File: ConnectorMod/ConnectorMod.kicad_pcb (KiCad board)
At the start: 2 copper layers, 98.5 x 90 mm, 82 parts, among them J1 PJ-325, J10 VIN, J11 VCC, J12 MRX, J13 MTX, J14 DACL, J15 DACR, J16 DACG, J17 VSW, J2 PJ-325, J3 PJ-325, J4 PJ-066A, J5 BAT1, J6 BAT2, J7 AMP, J8 GNDA, J9 GND, Q1 MMBT3904, Q2 MMBT3904, Q3 MMBT3906, U1 TLP2366, U2 74LVC1G08, U3 TLV2372

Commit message: Remove loud jumper and tweak filter values
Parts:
- removed the C13 at (79.0, 77.5)
- removed the JP7 at (71.5, 74.5)
- removed JP8: LOUD_R, project-parts:SolderJumper_Custom
- removed the R19 at (67.0, 82.0)
- removed the R20 at (54.0, 82.0)
- removed the R21 at (78.0, 74.5)
- removed the R22 at (80.0, 74.5)
- added C8: 330p, Capacitor_SMD:C_0603_1608Metric, F.Cu at (66.5, 86.0)
- added C9: 330p, Capacitor_SMD:C_0603_1608Metric, F.Cu at (54.5, 86.0)
- C6, C7: value 1n -> 330p
- moved R16 45.7 mm to (98.0, 72.0), turned to 0 degrees
- moved R15 29.8 mm to (91.5, 72.0), turned to 180 degrees
- moved C6 0.50 mm to (66.5, 84.0)
- moved C7 0.50 mm to (54.5, 84.0)
- renumbered C8 to C10, C9 to C11, C10 to C12, C11 to C13, C12 to C15, JP9 to JP7, R17 to R15, R18 to R16, R15 to R17, R16 to R18, R23 to R19, R24 to R20, R25 to R21, R26 to R22, R27 to R23, R28 to R24
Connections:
- C12 pad 1: Net-(C10-Pad1) -> Net-(U3A--)
- C12 pad 2: Net-(C10-Pad2) -> Net-(C12-Pad2)
- C13 pad 1: Net-(C11-Pad1) -> Net-(U3B--)
- C13 pad 2: Net-(C11-Pad2) -> Net-(C13-Pad2)
- C6 pad 1: Net-(C10-Pad1) -> Net-(U3A--)
- C7 pad 1: Net-(C11-Pad1) -> Net-(U3B--)
- R13 pad 1: Net-(C10-Pad2) -> Net-(C12-Pad2)
- R14 pad 1: Net-(C11-Pad2) -> Net-(C13-Pad2)
- R15 pad 1: Net-(C10-Pad1) -> Net-(C12-Pad2)
- R15 pad 2: Net-(U3A--) -> GNDA
- R16 pad 1: Net-(C11-Pad1) -> Net-(C13-Pad2)
- R16 pad 2: Net-(U3B--) -> GNDA
- U3 pad 1: Net-(C10-Pad1) -> Net-(U3A--)
- U3 pad 7: Net-(C11-Pad1) -> Net-(U3B--)
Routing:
- net Net-(C11-Pad1): track 52.4 -> 0.00 mm
- net Net-(U3B--): track 7.52 -> 55.3 mm
- net Net-(C10-Pad1): track 34.7 -> 0.00 mm
- net Net-(U3A--): track 7.38 -> 37.2 mm
- net Net-(JP8-A): track 18.6 -> 0.00 mm, vias 2 -> 0
- net /VCENT: track 15.4 -> 0.00 mm
- net Net-(C13-Pad2): track 0.00 -> 10.4 mm
- net Net-(JP7-A): track 7.89 -> 0.00 mm
- net +3.3VA: track 48.7 -> 41.4 mm
- net Net-(C12-Pad2): track 0.00 -> 7.32 mm
- net Net-(C11-Pad2): track 4.72 -> 0.00 mm
- net Net-(C10-Pad2): track 4.72 -> 0.00 mm
- net +6V: track 77.5 -> 75.5 mm
- net Net-(C7-Pad2): track 7.99 -> 9.49 mm
- net Net-(C6-Pad2): track 7.99 -> 9.49 mm
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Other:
- board text added: "${TITLE} ${REVISION}"
- board text removed: "${TITLE} v${REVISION}"
- board text removed: "LOUD"

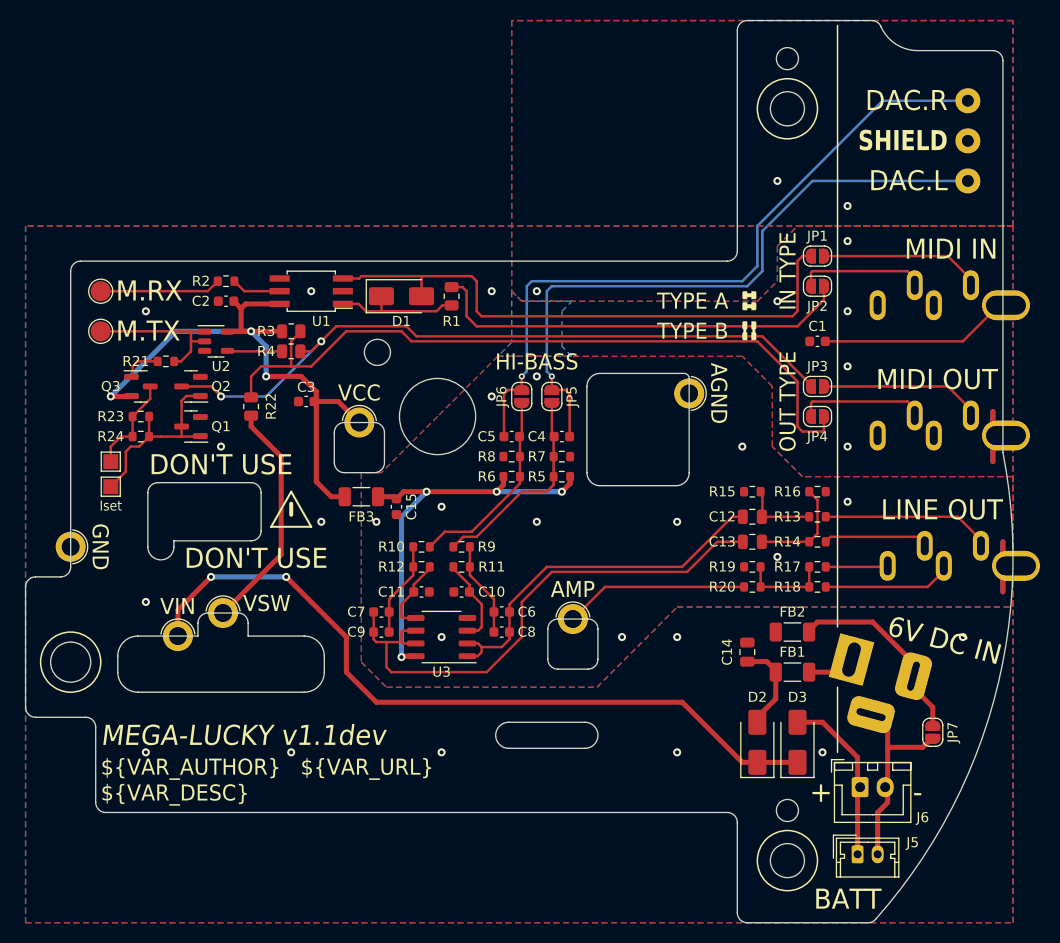
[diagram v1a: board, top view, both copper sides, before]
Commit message: Adjust outline and holes
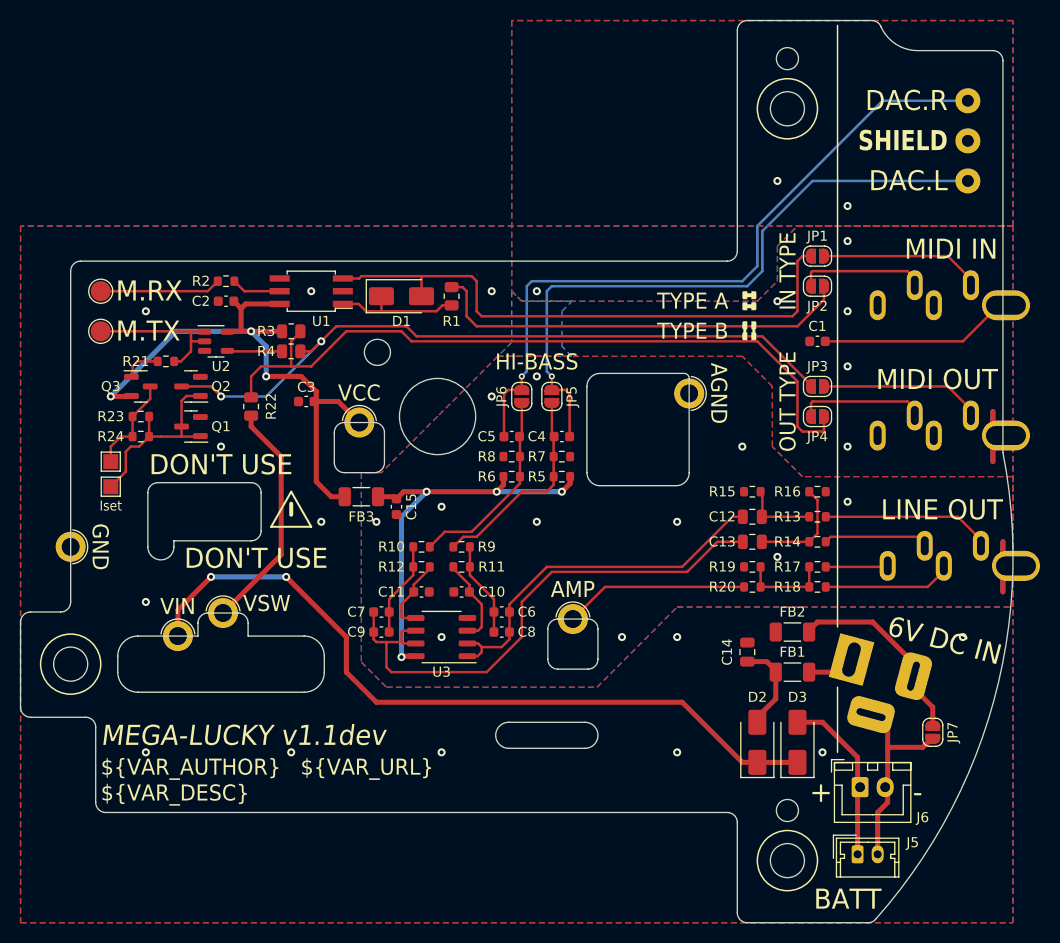
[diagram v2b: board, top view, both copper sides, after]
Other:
- board size 98.5 x 90 mm -> 99 x 90 mm

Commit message: Change MIDI type jumpers to cross pads
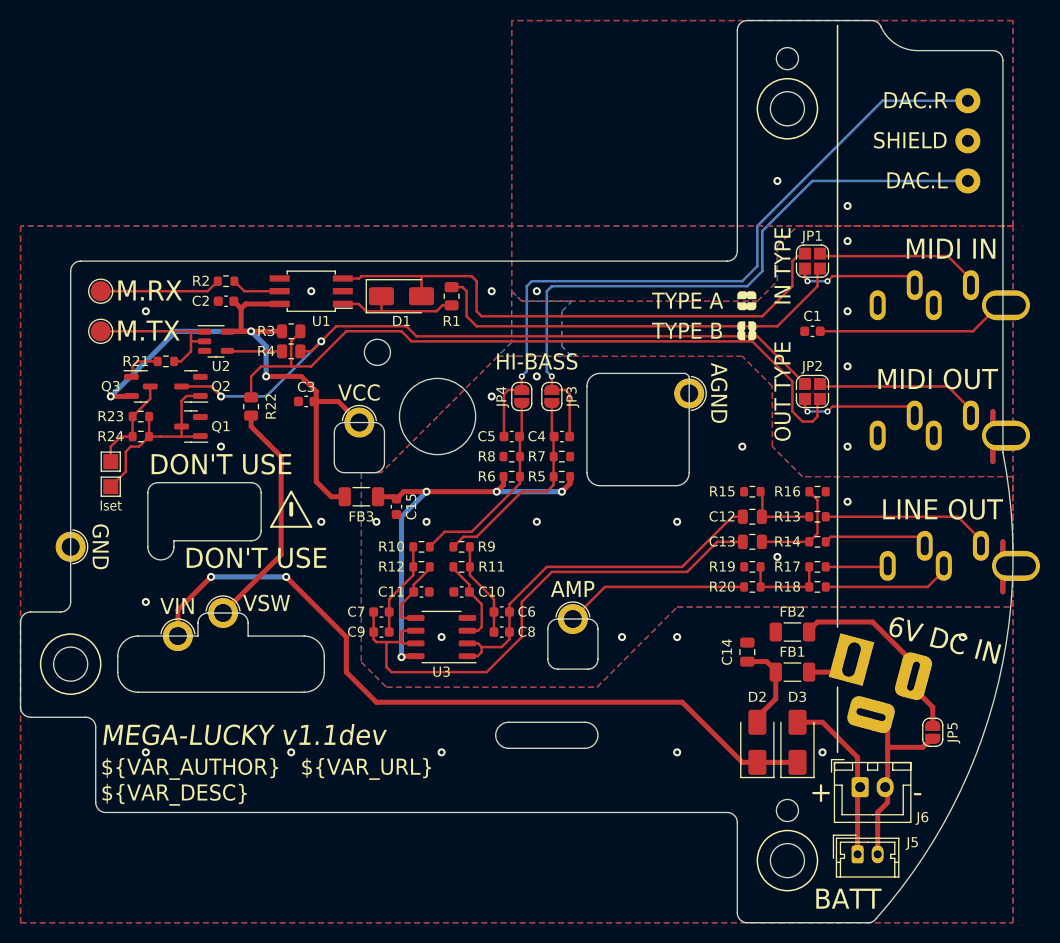
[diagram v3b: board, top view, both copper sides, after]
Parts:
- removed the JP3 at (98.0, 61.5)
- removed the JP4 at (98.0, 64.5)
- JP1: value MIT -> XMI; footprint project-parts:SolderJumper_Custom -> project-parts:SolderJumper_Cross
- JP2: value MIR -> XMO; footprint project-parts:SolderJumper_Custom -> project-parts:SolderJumper_Cross
- moved JP2 10.5 mm to (97.5, 62.0)
- moved C1 1.12 mm to (97.5, 56.0)
- moved JP1 0.71 mm to (97.5, 49.0)
- renumbered JP5 to JP3, JP6 to JP4, JP7 to JP5
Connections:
- net /MIN_G renamed Net-(C1-Pad1)
- JP2 pad 1: /MIN_R -> /MOUT_SINK
- JP2 pad 2: /MIN_SRC -> /MOUT_T
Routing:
- net /MIN_SINK: track 57.6 -> 55.7 mm
- net /MOUT_SRC: track 73.2 -> 71.9 mm
- net /MOUT_SINK: track 71.2 -> 70.4 mm
- net /MOUT_T: track 16.2 -> 16.7 mm
- net /MIN_T: track 16.2 -> 16.7 mm
- net /MIN_R: vias 0 -> 2
- net /MOUT_R: vias 0 -> 2
- net GND: vias 18 -> 17

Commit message: Use protected source/sink for MIDI out
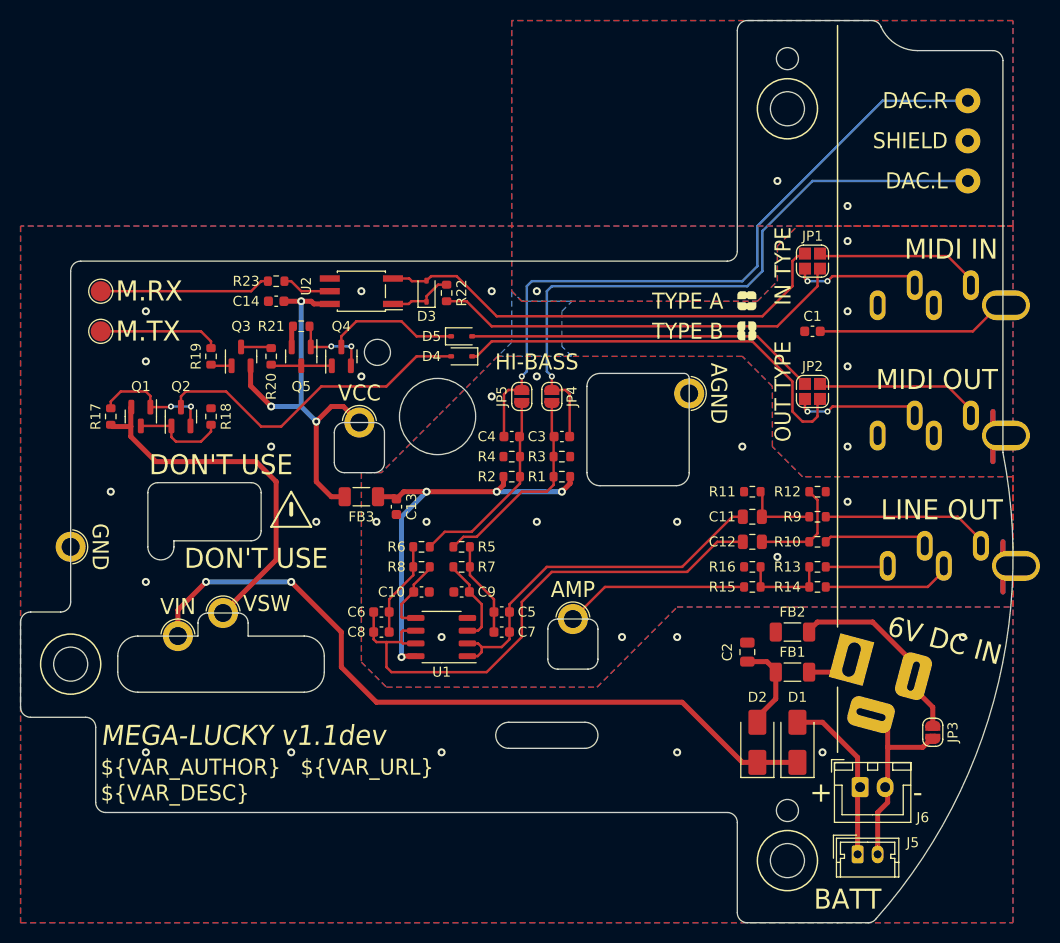
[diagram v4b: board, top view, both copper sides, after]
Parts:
- removed the C3 at (47.0, 63.0)
- removed the D1 at (56.5, 52.5)
- removed the R1 at (61.5, 52.5)
- removed the R23 at (30.5, 64.5)
- removed the R3 at (45.5, 56.0)
- removed the R4 at (45.5, 58.0)
- removed TP1, TP2: Iset, TestPoint:TestPoint_Pad_1.5x1.5mm
- removed the U2 at (38.0, 57.0)
- added D3: BAT54WS, Diode_SMD:D_SOD-323, F.Cu at (59.0, 52.0)
- added D4: BAT54WS, Diode_SMD:D_SOD-323, F.Cu at (62.5, 58.5)
- added D5: BAT54WS, Diode_SMD:D_SOD-323, F.Cu at (62.5, 56.5)
- added Q2: MMBT3906, Package_TO_SOT_SMD:SOT-23, F.Cu at (34.5, 64.5)
- added Q3: MMBT3906, Package_TO_SOT_SMD:SOT-23, F.Cu at (40.5, 58.5)
- added R17: 100R, Resistor_SMD:R_0603_1608Metric, F.Cu at (27.5, 64.5)
- added R18: 10K, Resistor_SMD:R_0603_1608Metric, F.Cu at (37.5, 64.5)
- added R20: 10K, Resistor_SMD:R_0603_1608Metric, F.Cu at (43.5, 58.5)
- R21: renamed from R24; value 1K -> 100R
- R22: footprint Resistor_SMD:R_0805_2012Metric -> Resistor_SMD:R_0603_1608Metric
- U2: renamed from U1; footprint Package_SO:SO-6_4.4x3.6mm_P1.27mm -> Package_SO:SO-5_4.4x3.6mm_P1.27mm
- moved R22 22.6 mm to (61.0, 52.2)
- moved R21 19.4 mm to (46.5, 55.5), turned to 180 degrees
- moved Q4 15.3 mm to (50.5, 58.5), turned to 90 degrees
- moved Q5 13.0 mm to (46.5, 58.5), turned to -90 degrees
- moved C14 5.00 mm to (44.0, 53.0)
- moved R23 5.00 mm to (44.0, 51.0)
- moved U2 5.00 mm to (52.5, 52.0)
- moved R19 4.53 mm to (37.5, 58.5), turned to -90 degrees
- moved Q1 3.00 mm to (30.5, 64.5), turned to -90 degrees
- renumbered C11 to C10, C12 to C11, C13 to C12, C15 to C13, C2 to C14, C14 to C2, C4 to C3, C5 to C4, C6 to C5, C7 to C6, C8 to C7, C9 to C8, C10 to C9, D3 to D1, JP5 to JP3, JP3 to JP4, JP4 to JP5, J7 to PAD1, J15 to PAD10, J16 to PAD11, J8 to PAD2, J9 to PAD3, J10 to PAD4, J11 to PAD5, J17 to PAD6, J12 to PAD7, J13 to PAD8, J14 to PAD9, Q3 to Q1, Q2 to Q4, Q1 to Q5, R5 to R1, R14 to R10, R15 to R11, R16 to R12, R17 to R13, R18 to R14, R20 to R15, R19 to R16, R21 to R19, R6 to R2, R2 to R23, R7 to R3, R8 to R4, R9 to R5, R10 to R6, R11 to R7, R12 to R8, R13 to R9, U3 to U1
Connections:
- Q1 pad 1: Net-(Q3-B) -> Net-(Q1-B)
- Q1 pad 2: +3.3V -> +VSW
- Q1 pad 3: Net-(Q3-C) -> Net-(Q1-C)
- Q4 pad 1: Net-(Q1-B) -> Net-(Q4-B)
- Q4 pad 2: GND -> Net-(Q4-E)
- Q4 pad 3: /MOUT_SINK -> Net-(D5-K)
- Q5 pad 1: Net-(Q1-B) -> Net-(Q4-E)
- Q5 pad 3: Net-(Q1-B) -> Net-(Q4-B)
- R21 pad 1: Net-(Q3-C) -> Net-(Q4-E)
- R21 pad 2: Net-(Q1-B) -> GND
- R22 pad 1: +VSW -> /MIN_SRC
- R22 pad 2: /MOUT_SRC -> Net-(D3-K)
- R23 pad 1: Net-(R2-Pad1) -> (no net)
- U2 pad 1: /MIN_SD -> Net-(D3-K)
- U2 pad 5: Net-(R2-Pad1) -> Net-(R23-Pad1)
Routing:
- net /MOUT_SINK: track 70.4 -> 35.2 mm, vias 2 -> 0
- net Net-(D4-A): track 0.00 -> 32.6 mm
- net /MOUT_SRC: track 71.9 -> 42.2 mm
- net +3.3V: track 60.4 -> 40.3 mm
- net +VSW: track 23.3 -> 36.7 mm
- net Net-(D5-K): track 0.00 -> 13.3 mm
- net /MIN_SD: track 12.9 -> 0.00 mm
- net Net-(Q1-C): track 0.00 -> 9.39 mm
- net /MIN_SINK: track 55.7 -> 47.1 mm
- net Net-(Q4-E): track 0.00 -> 8.15 mm, vias 0 -> 2
- net Net-(Q1-B): track 19.9 -> 12.4 mm, vias 0 -> 2
- net Net-(Q3-C): track 9.82 -> 3.05 mm
- net Net-(D3-K): track 0.00 -> 6.51 mm
- net Net-(Q4-B): track 0.00 -> 6.10 mm
- net Net-(R4-Pad1): track 5.47 -> 0.00 mm
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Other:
- board text removed: "Iset"

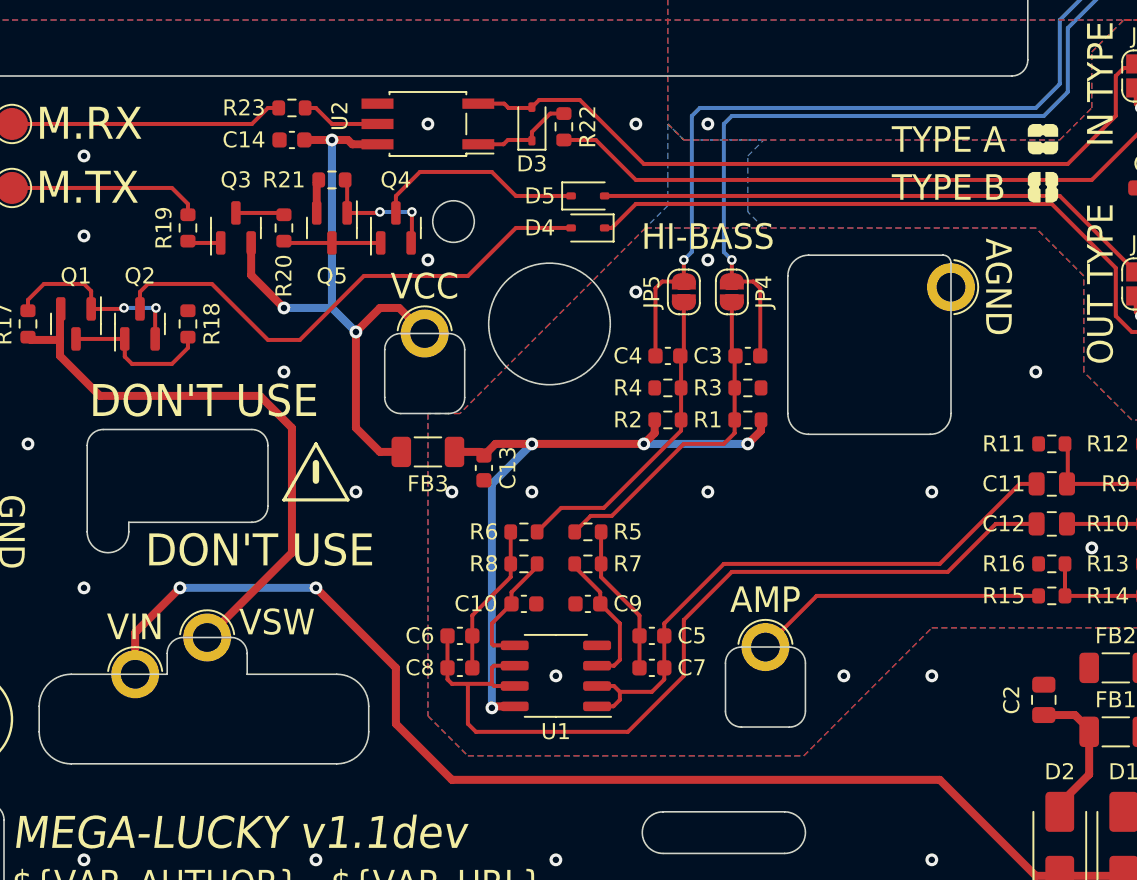
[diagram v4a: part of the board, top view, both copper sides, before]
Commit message: Tidy up opamp circuit
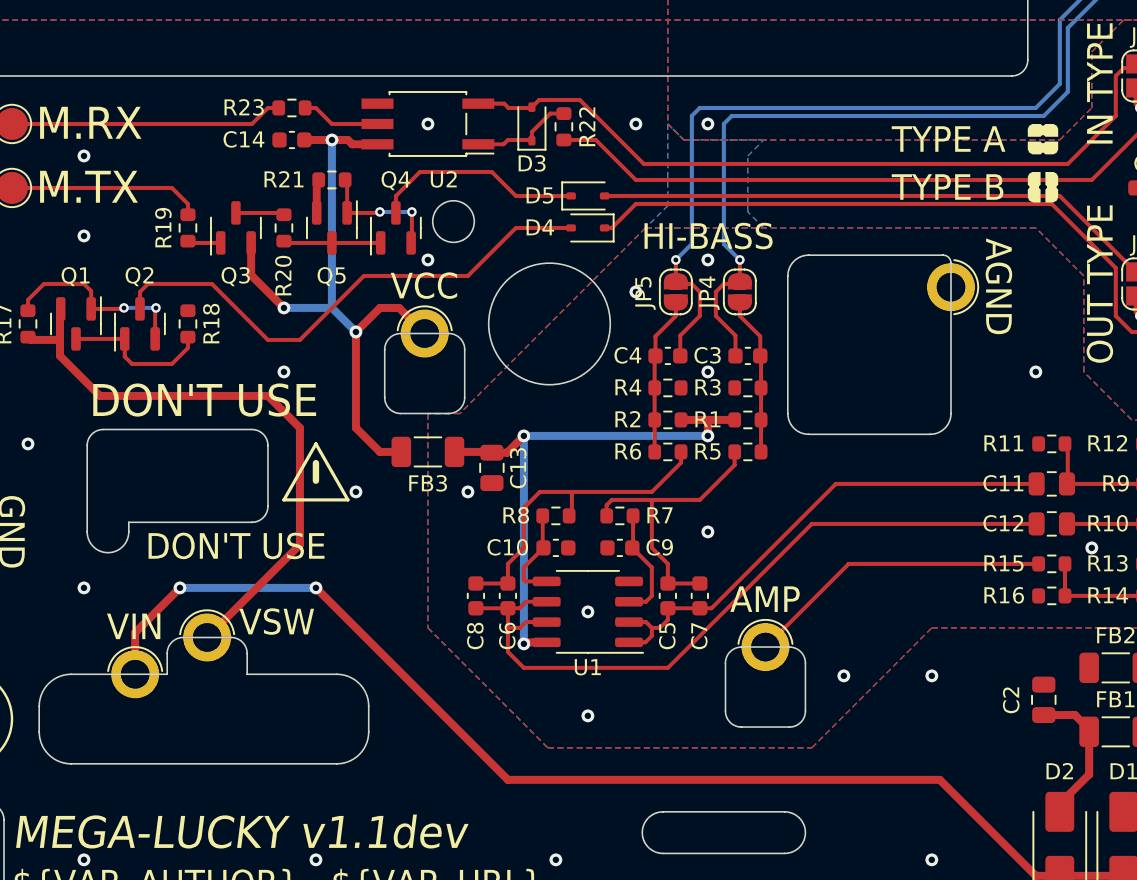
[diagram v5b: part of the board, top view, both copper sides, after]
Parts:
- C11, C12: value 10u -> 1u
- C13: value 100n -> 1u; footprint Capacitor_SMD:C_0603_1608Metric -> Capacitor_SMD:C_0805_2012Metric
- moved R5 11.2 mm to (72.5, 72.5), turned to 180 degrees
- moved R6 10.3 mm to (67.5, 72.5), turned to 0 degrees
- moved C7 5.41 mm to (69.5, 81.5), turned to 90 degrees
- moved C8 4.61 mm to (55.5, 81.5), turned to 90 degrees
- moved U1 4.47 mm to (62.5, 82.5)
- moved C10 4.03 mm to (60.5, 78.5)
- moved C9 4.03 mm to (64.5, 78.5)
- moved C6 3.91 mm to (57.5, 81.5), turned to 90 degrees
- moved R7 3.61 mm to (64.5, 76.5), turned to 0 degrees
- moved R8 3.61 mm to (60.5, 76.5), turned to 180 degrees
- moved C5 2.69 mm to (67.5, 81.5), turned to 90 degrees
- moved R15 2.00 mm to (91.5, 79.5)
- moved R16 2.00 mm to (91.5, 81.5)
- moved C13 0.50 mm to (56.5, 73.5)
- moved JP4 0.50 mm to (72.0, 62.5)
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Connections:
- R23 pad 1: (no net) -> Net-(R23-Pad1)
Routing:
- net Net-(JP4-B): track 20.8 -> 9.90 mm
- net Net-(C6-Pad2): track 9.49 -> 20.4 mm
- net Net-(JP5-B): track 19.8 -> 9.90 mm
- net Net-(C5-Pad2): track 9.49 -> 18.2 mm
- net Net-(U1B--): track 55.3 -> 47.1 mm
- net +3.3VA: track 41.4 -> 35.1 mm, vias 4 -> 3
- net Net-(U1A--): track 37.2 -> 31.4 mm
- net +6V: track 75.1 -> 73.0 mm
- net Net-(U1A-+): track 8.75 -> 7.10 mm
- net Net-(U1B-+): track 7.63 -> 5.99 mm
- net /AMP: track 18.4 -> 19.2 mm
- net +VSW: track 36.7 -> 37.4 mm
